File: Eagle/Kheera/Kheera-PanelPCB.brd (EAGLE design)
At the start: 42.9 x 80 mm, 5 parts, among them M1 RARNDT-MISCELANEOUS_FEATHERBO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

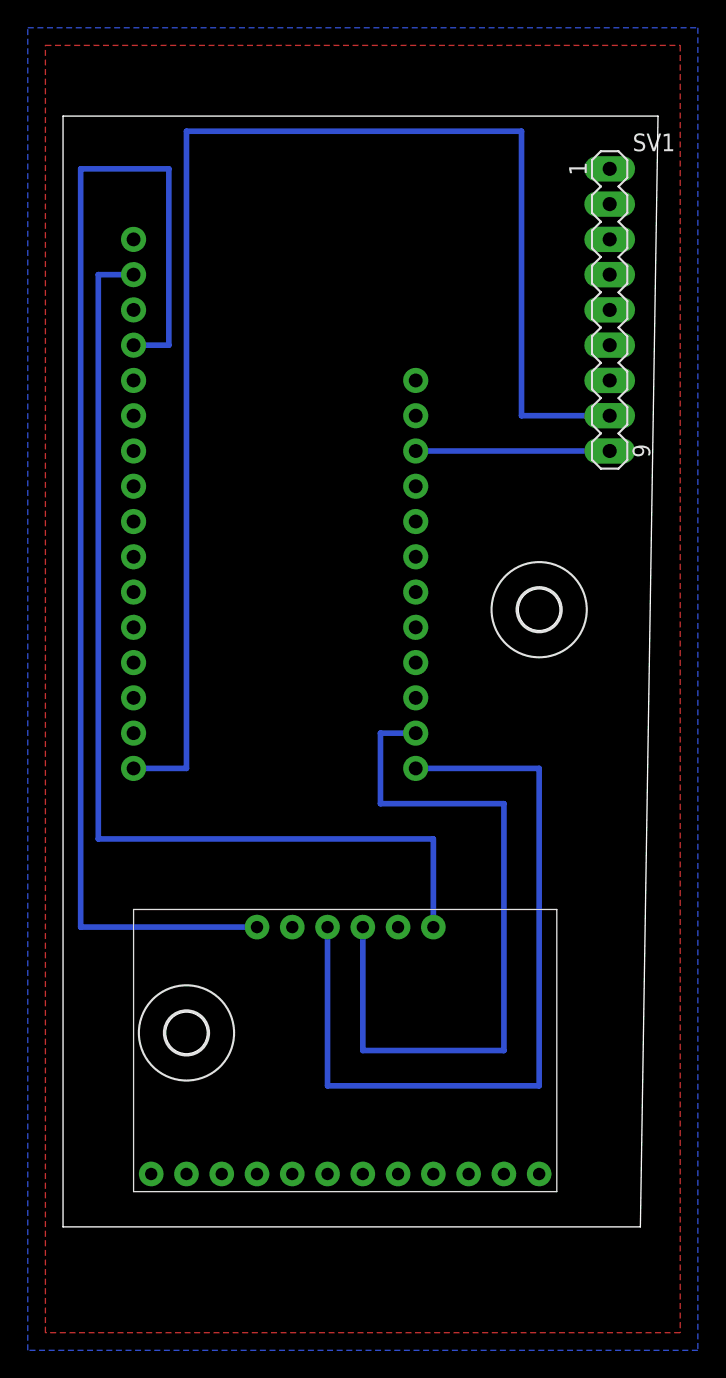
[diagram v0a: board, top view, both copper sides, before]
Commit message: Phase 2 of Kheera's Hand Model Final Print
> 3D print hand model accessing
> Redesign hand Model in Solidworks
> Smooth fingertips
> Test light diffusing
> Model needs hole for cord
> Design schematic / board
 > Arrange position for LED's 
> Create final to do for phase 3 & move into production (printing final)
> Add final touches on SolidWorks Model
> Add final touches on Eagle Board & Schematic Design
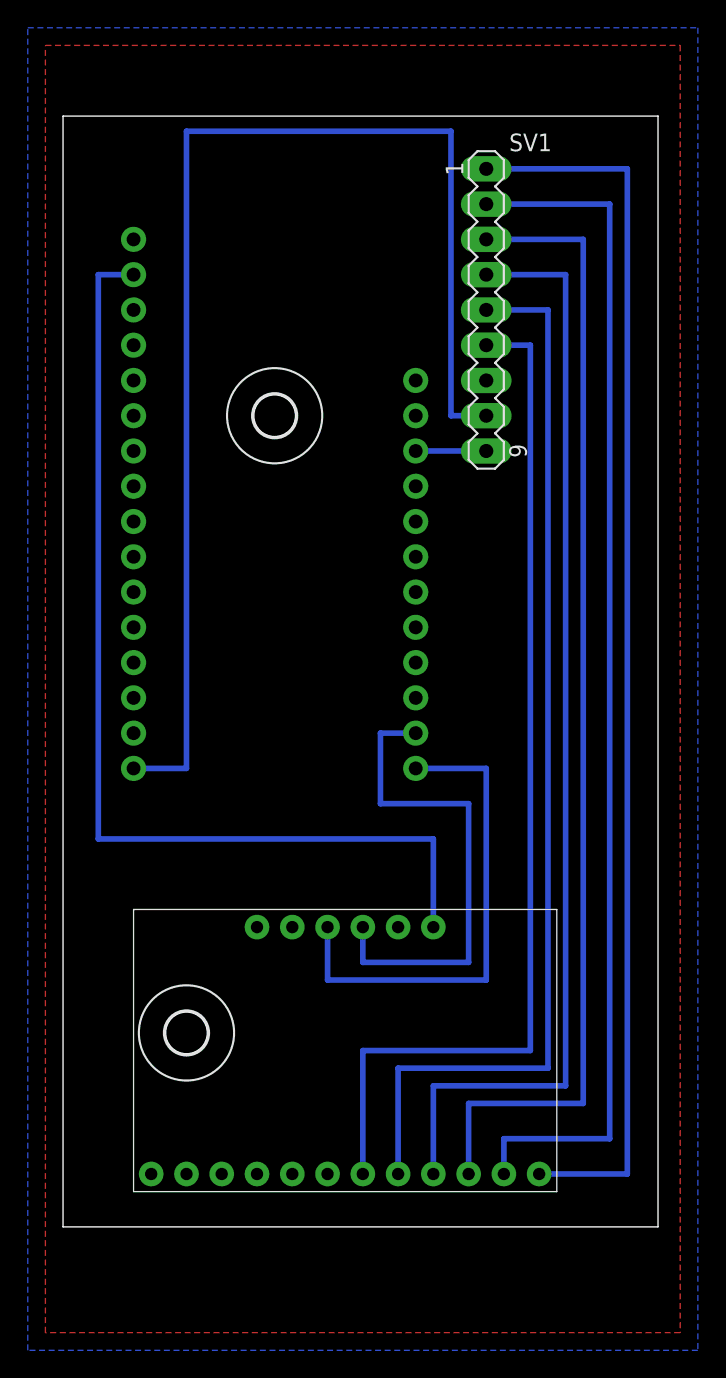
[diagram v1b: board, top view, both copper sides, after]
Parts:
- moved H1 23.6 mm to (15.2, 58.4)
- moved SV1 8.89 mm to (30.5, 66.0)
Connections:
- removed net TX: M1.15
- new net N$2: SV1.1, U$5.11
- new net N$3: SV1.2, U$5.10
- new net N$4: SV1.3, U$5.9
- new net N$5: SV1.4, U$5.8
- new net N$6: SV1.5, U$5.7
- new net N$7: SV1.6, U$5.6
- net GND: now also SV1.7
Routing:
- net N$2: track 0.00 -> 88.9 mm
- net GND: track 88.9 -> 0.00 mm
- net N$3: track 0.00 -> 86.4 mm
- net N$4: track 0.00 -> 82.6 mm
- net N$5: track 0.00 -> 80.0 mm
- net N$6: track 0.00 -> 77.5 mm
- net N$7: track 0.00 -> 74.9 mm
- net SDA: track 58.4 -> 35.6 mm
- net SCL: track 53.3 -> 35.6 mm
- net USB: track 14.0 -> 5.08 mm
- net N$1: track 100.7 -> 91.8 mm
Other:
- outline, holes or cut-outs redrawn
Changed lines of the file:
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@@
 <board>
 <plain>
-<wire x1="0" y1="0" x2="41.58" y2="0" width="0" layer="20"/>
-<wire x1="41.58" y1="0" x2="42.85" y2="80" width="0" layer="20"/>
+<wire x1="0" y1="0" x2="42.85" y2="0" width="0" layer="20"/>
+<wire x1="42.85" y1="0" x2="42.85" y2="80" width="0" layer="20"/>
 <wire x1="42.85" y1="80" x2="0" y2="80" width="0" layer="20"/>
 <wire x1="0" y1="80" x2="0" y2="0" width="0" layer="20"/>
+<dimension x1="0" y1="80" x2="42.85" y2="80" x3="21.425" y3="95.25" textsize="1.778" layer="1"/>
+<dimension x1="41.58" y1="0" x2="42.85" y2="80" x3="-12.676165625" y3="40.871396875" textsize="1.778" layer="1"/>
 </plain>
 <attributes>
@@
 <element name="M1" library="StewartPlatform" package="RARNDT-MISCELANEOUS_FEATHERBOARD_ESP32" value="RARNDT-MISCELANEOUS_FEATHERBOARD_ESP32FETHERWING_DIM_ESP32" x="15.24" y="52.07" smashed="yes" rot="R270"/>
 <element name="U$5" library="MS-121" package="MS-121" value="MS-121" x="20.32" y="12.7" smashed="yes" rot="R270"/>
-<element name="SV1" library="con-lstb" library_urn="urn:adsk.eagle:library:162" package="MA09-1" package3d_urn="urn:adsk.eagle:package:8350/1" value="" x="39.37" y="66.04" smashed="yes" rot="R270">
-<attribute name="MF" value="" x="39.37" y="66.04" size="1.778" layer="27" rot="R270" display="off"/>
-<attribute name="MPN" value="" x="39.37" y="66.04" size="1.778" layer="27" rot="R270" display="off"/>
-<attribute name="NAME" x="41.021" y="77.47" size="1.27" layer="25" ratio="10"/>
-<attribute name="OC_FARNELL" value="unknown" x="39.37" y="66.04" size="1.778" layer="27" rot="R270" display="off"/>
-<attribute name="OC_NEWARK" value="unknown" x="39.37" y="66.04" size="1.778" layer="27" rot="R270" display="off"/>
-<attribute name="POPULARITY" value="0" x="39.37" y="66.04" size="1.778" layer="27" rot="R270" display="off"/>
-<attribute name="VALUE" x="36.449" y="66.04" size="1.27" layer="27" ratio="10" rot="R270"/>
+<element name="SV1" library="con-lstb" library_urn="urn:adsk.eagle:library:162" package="MA09-1" package3d_urn="urn:adsk.eagle:package:8350/1" value="" x="30.48" y="66.04" smashed="yes" rot="R270">
+<attribute name="MF" value="" x="30.48" y="66.04" size="1.778" layer="27" rot="R270" display="off"/>
+<attribute name="MPN" value="" x="30.48" y="66.04" size="1.778" layer="27" rot="R270" display="off"/>
+<attribute name="NAME" x="32.131" y="77.47" size="1.27" layer="25" ratio="10"/>
+<attribute name="OC_FARNELL" value="unknown" x="30.48" y="66.04" size="1.778" layer="27" rot="R270" display="off"/>
+<attribute name="OC_NEWARK" value="unknown" x="30.48" y="66.04" size="1.778" layer="27" rot="R270" display="off"/>
+<attribute name="POPULARITY" value="0" x="30.48" y="66.04" size="1.778" layer="27" rot="R270" display="off"/>
+<attribute name="VALUE" x="27.559" y="66.04" size="1.27" layer="27" ratio="10" rot="R270"/>
 </element>
 <element name="H2" library="holes" library_urn="urn:adsk.eagle:library:237" package="3,0" package3d_urn="urn:adsk.eagle:package:14277/1" value="MOUNT-HOLE3.0" x="8.89" y="13.97" smashed="yes">
 <attribute name="POPULARITY" value="3" x="-1.27" y="24.13" size="1.778" layer="27" display="off"/>
 </element>
-<element name="H1" library="holes" library_urn="urn:adsk.eagle:library:237" package="3,0" package3d_urn="urn:adsk.eagle:package:14277/1" value="MOUNT-HOLE3.0" x="34.29" y="44.45" smashed="yes">
-<attribute name="POPULARITY" value="3" x="24.13" y="53.34" size="1.778" layer="27" display="off"/>
+<element name="H1" library="holes" library_urn="urn:adsk.eagle:library:237" package="3,0" package3d_urn="urn:adsk.eagle:package:14277/1" value="MOUNT-HOLE3.0" x="15.24" y="58.42" smashed="yes">
+<attribute name="POPULARITY" value="3" x="5.08" y="67.31" size="1.778" layer="27" display="off"/>
 </element>
 </elements>
@@
 <contactref element="U$5" pad="GND"/>
 <contactref element="M1" pad="4"/>
-<wire x1="5.08" y1="63.5" x2="7.62" y2="63.5" width="0.4064" layer="16"/>
-<wire x1="7.62" y1="63.5" x2="7.62" y2="76.2" width="0.4064" layer="16"/>
-<wire x1="7.62" y1="76.2" x2="1.27" y2="76.2" width="0.4064" layer="16"/>
-<wire x1="1.27" y1="76.2" x2="1.27" y2="21.59" width="0.4064" layer="16"/>
-<wire x1="1.27" y1="21.59" x2="13.97" y2="21.59" width="0.4064" layer="16"/>
+<contactref element="SV1" pad="7"/>
+<wire x1="5.08" y1="63.5" x2="30.48" y2="60.96" width="0" layer="19" extent="1-1"/>
+<wire x1="13.97" y1="21.59" x2="30.48" y2="60.96" width="0" layer="19" extent="1-1"/>
 </signal>
 <signal name="3V3">
@@
 <wire x1="26.67" y1="27.94" x2="26.67" y2="21.59" width="0.4064" layer="16"/>
 </signal>
-<signal name="TX">
-<contactref element="M1" pad="15"/>
-</signal>
 <signal name="SCL">
 <contactref element="M1" pad="18"/>
 <contactref element="U$5" pad="SCL"/>
-<wire x1="31.75" y1="12.7" x2="21.59" y2="12.7" width="0.4064" layer="16"/>
-<wire x1="21.59" y1="21.59" x2="21.59" y2="12.7" width="0.4064" layer="16"/>
-<wire x1="31.75" y1="12.7" x2="31.75" y2="30.48" width="0.4064" layer="16"/>
-<wire x1="31.75" y1="30.48" x2="22.86" y2="30.48" width="0.4064" layer="16"/>
+<wire x1="29.21" y1="19.05" x2="21.59" y2="19.05" width="0.4064" layer="16"/>
+<wire x1="21.59" y1="21.59" x2="21.59" y2="19.05" width="0.4064" layer="16"/>
+<wire x1="29.21" y1="19.05" x2="29.21" y2="30.48" width="0.4064" layer="16"/>
+<wire x1="29.21" y1="30.48" x2="22.86" y2="30.48" width="0.4064" layer="16"/>
 <wire x1="22.86" y1="30.48" x2="22.86" y2="35.56" width="0.4064" layer="16"/>
 <wire x1="22.86" y1="35.56" x2="25.4" y2="35.56" width="0.4064" layer="16"/>
@@
 <contactref element="M1" pad="17"/>
 <contactref element="U$5" pad="SDA"/>
-<wire x1="34.29" y1="10.16" x2="19.05" y2="10.16" width="0.4064" layer="16"/>
-<wire x1="19.05" y1="21.59" x2="19.05" y2="10.16" width="0.4064" layer="16"/>
-<wire x1="34.29" y1="10.16" x2="34.29" y2="33.02" width="0.4064" layer="16"/>
-<wire x1="34.29" y1="33.02" x2="25.4" y2="33.02" width="0.4064" layer="16"/>
+<wire x1="30.48" y1="17.78" x2="19.05" y2="17.78" width="0.4064" layer="16"/>
+<wire x1="19.05" y1="21.59" x2="19.05" y2="17.78" width="0.4064" layer="16"/>
+<wire x1="30.48" y1="17.78" x2="30.48" y2="33.02" width="0.4064" layer="16"/>
+<wire x1="30.48" y1="33.02" x2="25.4" y2="33.02" width="0.4064" layer="16"/>
 </signal>
 <signal name="N$1">
@@
 <wire x1="5.08" y1="33.02" x2="8.89" y2="33.02" width="0.4064" layer="16"/>
 <wire x1="8.89" y1="33.02" x2="8.89" y2="78.9078" width="0.4064" layer="16"/>
-<wire x1="8.89" y1="78.9078" x2="33.02" y2="78.9078" width="0.4064" layer="16"/>
-<wire x1="33.02" y1="78.9078" x2="33.02" y2="58.42" width="0.4064" layer="16"/>
-<wire x1="33.02" y1="58.42" x2="39.37" y2="58.42" width="0.4064" layer="16"/>
+<wire x1="8.89" y1="78.9078" x2="27.94" y2="78.9078" width="0.4064" layer="16"/>
+<wire x1="27.94" y1="78.9078" x2="27.94" y2="58.42" width="0.4064" layer="16"/>
+<wire x1="27.94" y1="58.42" x2="30.48" y2="58.42" width="0.4064" layer="16"/>
 </signal>
 <signal name="USB">
 <contactref element="M1" pad="26"/>
 <contactref element="SV1" pad="9"/>
-<wire x1="25.4" y1="55.88" x2="39.37" y2="55.88" width="0.4064" layer="16"/>
+<wire x1="25.4" y1="55.88" x2="30.48" y2="55.88" width="0.4064" layer="16"/>
+</signal>
+<signal name="N$2">
+<contactref element="U$5" pad="11"/>
+<contactref element="SV1" pad="1"/>
+<wire x1="34.29" y1="3.81" x2="40.64" y2="3.81" width="0.4064" layer="16"/>
+<wire x1="40.64" y1="3.81" x2="40.64" y2="76.2" width="0.4064" layer="16"/>
+<wire x1="40.64" y1="76.2" x2="30.48" y2="76.2" width="0.4064" layer="16"/>
+</signal>
+<signal name="N$4">
+<contactref element="U$5" pad="9"/>
+<contactref element="SV1" pad="3"/>
+<wire x1="29.21" y1="3.81" x2="29.21" y2="8.89" width="0.4064" layer="16"/>
+<wire x1="29.21" y1="8.89" x2="37.465" y2="8.89" width="0.4064" layer="16"/>
+<wire x1="37.465" y1="8.89" x2="37.465" y2="71.12" width="0.4064" layer="16"/>
+<wire x1="37.465" y1="71.12" x2="30.48" y2="71.12" width="0.4064" layer="16"/>
+</signal>
+<signal name="N$5">
+<contactref element="U$5" pad="8"/>
+<contactref element="SV1" pad="4"/>
+<wire x1="26.67" y1="3.81" x2="26.67" y2="10.16" width="0.4064" layer="16"/>
+<wire x1="26.67" y1="10.16" x2="36.195" y2="10.16" width="0.4064" layer="16"/>
+<wire x1="36.195" y1="10.16" x2="36.195" y2="68.58" width="0.4064" layer="16"/>
+<wire x1="36.195" y1="68.58" x2="30.48" y2="68.58" width="0.4064" layer="16"/>
+</signal>
+<signal name="N$6">
+<contactref element="U$5" pad="7"/>
+<contactref element="SV1" pad="5"/>
+<wire x1="24.13" y1="3.81" x2="24.13" y2="11.43" width="0.4064" layer="16"/>
+<wire x1="24.13" y1="11.43" x2="34.925" y2="11.43" width="0.4064" layer="16"/>
+<wire x1="34.925" y1="11.43" x2="34.925" y2="66.04" width="0.4064" layer="16"/>
+<wire x1="34.925" y1="66.04" x2="30.48" y2="66.04" width="0.4064" layer="16"/>
+</signal>
+<signal name="N$7">
+<contactref element="U$5" pad="6"/>
+<contactref element="SV1" pad="6"/>
+<wire x1="21.59" y1="3.81" x2="21.59" y2="12.7" width="0.4064" layer="16"/>
+<wire x1="21.59" y1="12.7" x2="33.655" y2="12.7" width="0.4064" layer="16"/>
+<wire x1="33.655" y1="12.7" x2="33.655" y2="63.5" width="0.4064" layer="16"/>
+<wire x1="33.655" y1="63.5" x2="30.48" y2="63.5" width="0.4064" layer="16"/>
+</signal>
+<signal name="N$3">
+<contactref element="U$5" pad="10"/>
+<contactref element="SV1" pad="2"/>
+<wire x1="31.75" y1="3.81" x2="31.75" y2="6.35" width="0.4064" layer="16"/>
+<wire x1="31.75" y1="6.35" x2="39.37" y2="6.35" width="0.4064" layer="16"/>
+<wire x1="39.37" y1="6.35" x2="39.37" y2="73.66" width="0.4064" layer="16"/>
+<wire x1="39.37" y1="73.66" x2="30.48" y2="73.66" width="0.4064" layer="16"/>
 </signal>
 </signals>
